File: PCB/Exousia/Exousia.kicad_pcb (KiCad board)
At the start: 2 copper layers, 73 parts, among them J1 IN/out, J2 I2C buss, J3 in/OUT, Q1 2N7002, Q2 2N7002, Q3 2N7002, U1 AON7410, U2 AON7410, U3 RVSPG, U4 AON7410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

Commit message: started layout of PCB, minus main inductor :C
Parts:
- moved R16 112.1 mm to (161.0, 218.4)
- moved JP4 108.2 mm to (168.4, 215.6), turned to 180 degrees
- moved JP3 105.1 mm to (160.5, 214.6), turned to 180 degrees
- moved R3 104.9 mm to (134.9, 206.0), turned to 270 degrees
- moved R8 104.4 mm to (143.3, 207.0), turned to 270 degrees
- moved Q2 99.5 mm to (143.0, 210.8)
- moved R11 96.7 mm to (151.9, 208.8), turned to 270 degrees
- moved JP1 96.5 mm to (125.7, 200.9)
- moved R12 96.0 mm to (154.4, 206.2), turned to 270 degrees
- moved R19 95.4 mm to (168.7, 218.7)
- moved Q1 92.6 mm to (133.9, 210.3)
- moved D1 90.2 mm to (137.4, 209.0), turned to 90 degrees
- moved D4 88.7 mm to (154.4, 210.8), turned to 90 degrees
- moved R15 87.3 mm to (160.5, 206.0), turned to 270 degrees
- moved R26 84.7 mm to (122.2, 173.5)
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
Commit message: did a little bit of layout
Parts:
- moved J2 59.6 mm to (180.8, 166.4), turned to 180 degrees
- moved R26 55.5 mm to (176.0, 160.0), turned to 270 degrees
- moved R27 52.3 mm to (177.8, 160.0), turned to 270 degrees
- moved JP1 39.9 mm to (137.7, 162.8)
- moved R16 39.3 mm to (168.1, 179.8)
- moved R19 39.0 mm to (172.2, 179.8)
- moved JP4 38.8 mm to (172.5, 177.0)
- moved Q3 38.3 mm to (159.8, 175.0)
- moved JP3 38.3 mm to (167.9, 177.0)
- moved R18 37.8 mm to (172.2, 169.2), turned to 0 degrees
- moved R15 37.6 mm to (168.1, 169.2), turned to 180 degrees
- moved R11 37.4 mm to (159.5, 172.2), turned to 180 degrees
- moved Q1 37.4 mm to (146.1, 175.0)
- moved Q2 37.2 mm to (152.9, 175.0)
- moved D4 36.3 mm to (163.1, 175.5)
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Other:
- board text added: "main chip U3 is wrong footprint"

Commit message: did work
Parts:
- removed TP1: RVSPG, TestPoint:TestPoint_Loop_D2.50mm_Drill1.0mm
- removed TP2: FRWPG, TestPoint:TestPoint_Loop_D2.50mm_Drill1.0mm
- added L1: 2uH, Inductor_SMD:L_6.3x6.3_H3, F.Cu at (159.5, 147.3)
- D1, D3: value LED -> FRWPG
- D4: value LED -> RVSPG
- J3: footprint Connector_PinSocket_2.54mm:PinSocket_1x02_P2.54mm_Vertical -> Connector_PinSocket_2.54mm:PinSocket_1x04_P2.54mm_Vertical
- JP1: value SolderJumper_3_Open -> IO-Vselect; footprint Connector_PinSocket_2.54mm:PinSocket_1x03_P2.54mm_Vertical -> Jumper:SolderJumper-3_P1.3mm_Open_RoundedPad1.0x1.5mm_NumberLabels
- JP2: value SolderJumper_3_Open -> Pin_FRWEN / ADP; footprint Connector_PinSocket_2.54mm:PinSocket_1x03_P2.54mm_Vertical -> Jumper:SolderJumper-3_P1.3mm_Open_RoundedPad1.0x1.5mm_NumberLabels
- JP3: value SolderJumper_3_Open -> RVSEN; footprint Connector_PinSocket_2.54mm:PinSocket_1x03_P2.54mm_Vertical -> Jumper:SolderJumper-3_P1.3mm_Open_RoundedPad1.0x1.5mm_NumberLabels
- JP4: value SolderJumper_3_Open -> Pin_FRWEN; footprint Connector_PinSocket_2.54mm:PinSocket_1x03_P2.54mm_Vertical -> Jumper:SolderJumper-3_P1.3mm_Open_RoundedPad1.0x1.5mm_NumberLabels
- moved JP1 10.3 mm to (145.5, 169.4)
- moved J1 7.15 mm to (133.3, 153.9), turned to 180 degrees
- moved J3 7.12 mm to (190.2, 153.9), turned to 180 degrees
- moved R19 3.89 mm to (171.4, 176.0), turned to 180 degrees
- moved R16 3.81 mm to (168.1, 176.0)
- moved JP2 3.39 mm to (149.9, 153.2), turned to 180 degrees
- moved JP3 3.34 mm to (167.4, 173.7)
- moved JP4 3.31 mm to (172.2, 173.7)
- moved R18 2.41 mm to (171.4, 171.4)
- moved R15 2.29 mm to (168.1, 171.4)
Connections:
- J1 pad 2: Net-(D2-Pad1) -> GND
- J1 pad 3: (no net) -> Net-(D2-Pad1)
- J1 pad 4: (no net) -> Net-(D2-Pad1)
- J3 pad 2: Net-(J3-Pad2) -> GND
- R24 pad 1: Net-(J3-Pad2) -> Net-(J3-Pad3)
- R25 pad 2: Net-(J3-Pad2) -> Net-(J3-Pad3)

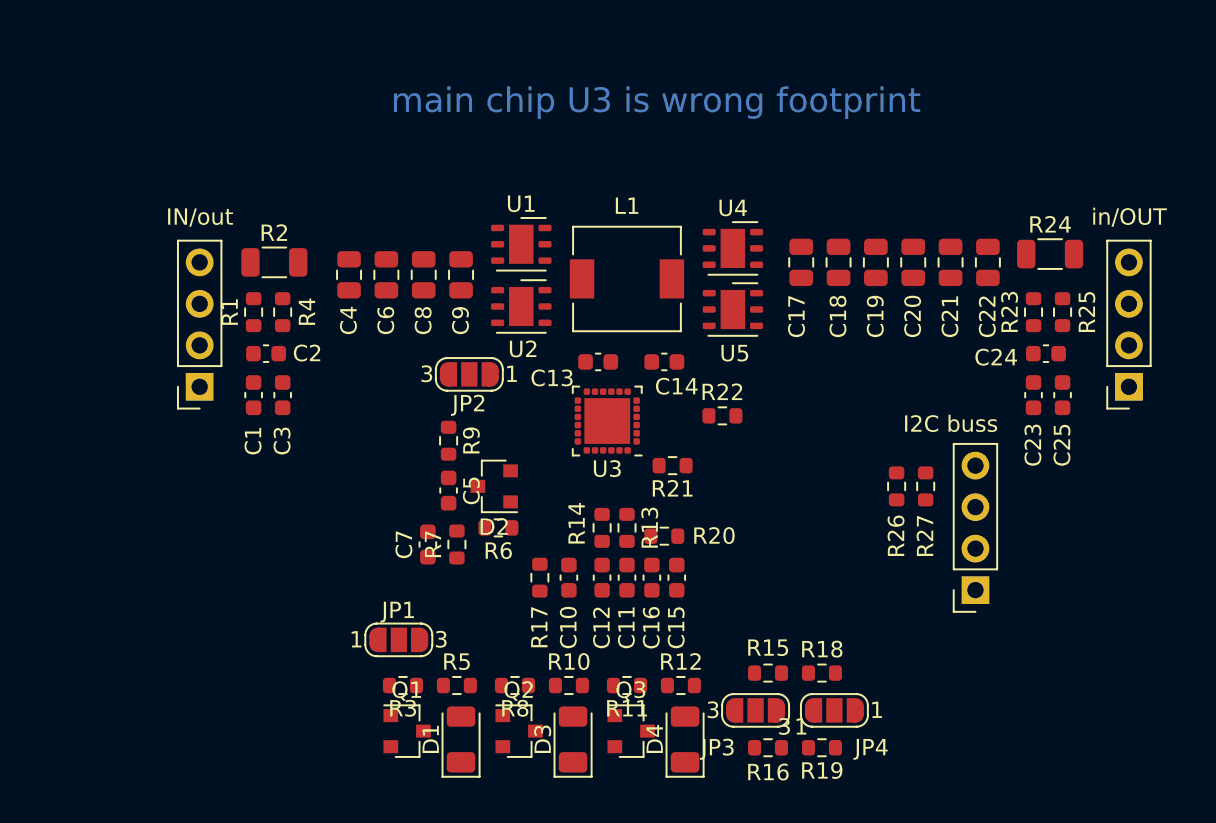
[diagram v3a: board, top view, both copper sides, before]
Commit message: updated some footrpints and compoinent valeus for 12A
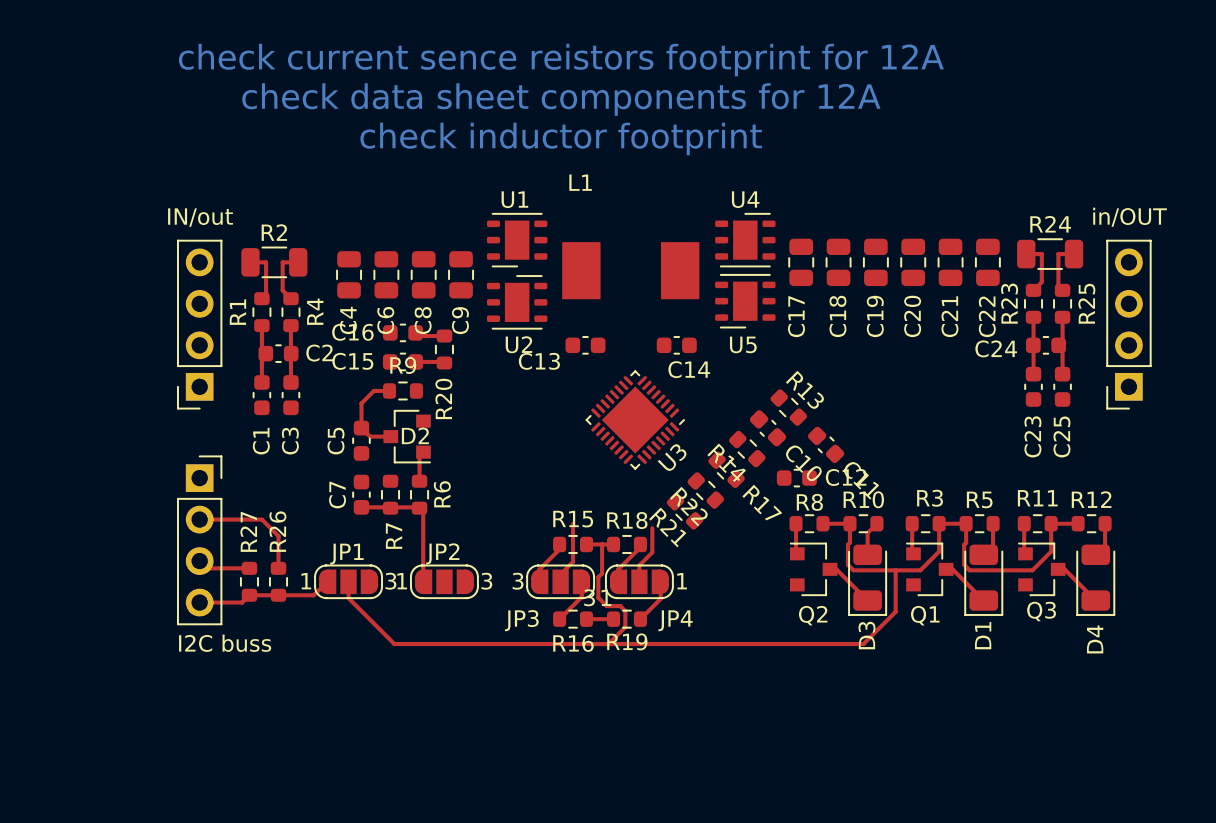
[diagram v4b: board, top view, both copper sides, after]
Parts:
- L1: value 2uH -> 0.82uH PIMB063T-R82MS-68; footprint Inductor_SMD:L_6.3x6.3_H3 -> PIMB063T-R82MS-68:PIMB063T-R82MS-68
- U3: footprint Package_DFN_QFN:TQFN-24-1EP_4x4mm_P0.5mm_EP2.8x2.8mm_PullBack -> Package_DFN_QFN:QFN-32-1EP_4x4mm_P0.4mm_EP2.9x2.9mm
- moved J2 48.0 mm to (133.3, 159.5), turned to 0 degrees
- moved R27 41.8 mm to (136.4, 165.9), turned to 90 degrees
- moved R26 38.3 mm to (138.2, 165.9), turned to 90 degrees
- moved R3 33.5 mm to (177.8, 162.3)
- moved D1 33.5 mm to (181.4, 165.6)
- moved Q1 33.5 mm to (178.1, 165.1)
- moved R5 33.5 mm to (181.1, 162.3)
- moved Q3 27.0 mm to (184.9, 165.1)
- moved R12 27.0 mm to (188.0, 162.3)
- moved D4 27.0 mm to (188.2, 165.6)
- moved R11 27.0 mm to (184.7, 162.3)
- moved C16 21.4 mm to (145.8, 150.6), turned to 180 degrees
- moved C15 21.3 mm to (145.8, 152.4), turned to 180 degrees
- moved Q2 20.6 mm to (170.9, 165.1)
- moved R10 20.6 mm to (174.0, 162.3)
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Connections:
- C10 pad 1: (no net) -> Net-(C10-Pad1)
- C15 pad 1: Net-(C15-Pad1) -> VDD
- JP1 pad 3: (no net) -> VDD
- R13 pad 1: (no net) -> Net-(R13-Pad1)
- R14 pad 1: (no net) -> Net-(R14-Pad1)
- R17 pad 1: (no net) -> Net-(R17-Pad1)
- R20 pad 2: Net-(C15-Pad1) -> VDD
- U3 pad 18: Net-(C15-Pad1) -> VDD
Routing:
- net Net-(JP1-Pad2): track 0.00 -> 74.5 mm
- net +3V3: track 0.00 -> 8.34 mm
- net Net-(C7-Pad1): track 0.00 -> 8.18 mm
- net SCL: track 0.00 -> 7.22 mm
- net Net-(C5-Pad1): track 0.00 -> 5.55 mm
- net Net-(D2-Pad1): track 0.00 -> 5.16 mm
- net RVSEN: track 0.00 -> 3.87 mm
- net Pin_FRWEN: track 0.00 -> 3.60 mm
- net Net-(C2-Pad1): track 0.00 -> 3.48 mm
- net Net-(C1-Pad2): track 0.00 -> 3.48 mm
- net Net-(C24-Pad1): track 0.00 -> 3.48 mm
- net Net-(C23-Pad2): track 0.00 -> 3.48 mm
- net Net-(C17-Pad1): track 0.00 -> 3.39 mm
- net Net-(C4-Pad1): track 0.00 -> 3.39 mm
- net Net-(J3-Pad3): track 0.00 -> 3.28 mm
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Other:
- board text added: "check current sence reistors footprint for 12A check data sheet components for 12A check inductor footprint"
- board text removed: "main chip U3 is wrong footprint"

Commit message: did routing!
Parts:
- moved C15 1.52 mm to (145.8, 153.9)
- moved C5 1.52 mm to (143.3, 158.8)
- moved C7 1.52 mm to (143.3, 162.1)
- moved D2 1.52 mm to (146.1, 158.5)
- moved R20 1.52 mm to (148.3, 153.2)
- moved R6 1.52 mm to (146.8, 162.1)
- moved R7 1.52 mm to (145.0, 162.1)
- moved R9 1.52 mm to (145.8, 155.7)
- moved C16 1.52 mm to (145.8, 152.1)
- moved J3 0.72 mm to (189.7, 153.4)
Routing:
- net Net-(U1-Pad4): track 0.00 -> 18.5 mm, vias 0 -> 2
- net Net-(C17-Pad1): track 3.39 -> 21.8 mm, vias 0 -> 2
- net Net-(U3-Pad5): track 0.00 -> 15.5 mm, vias 0 -> 2
- net Net-(D2-Pad1): track 5.16 -> 16.1 mm
- net Net-(C13-Pad1): track 0.00 -> 10.1 mm
- net Net-(U3-Pad7): track 0.00 -> 8.68 mm
- net Net-(U2-Pad4): track 0.00 -> 8.30 mm
- net Net-(R13-Pad1): track 0.00 -> 8.18 mm
- net GND: track 1.65 -> 9.41 mm, vias 0 -> 47
- net Net-(C14-Pad1): track 0.00 -> 7.56 mm
- net Net-(C10-Pad1): track 0.00 -> 6.88 mm
- net Net-(R14-Pad1): track 0.00 -> 5.57 mm
- net FRWPG: track 1.88 -> 6.83 mm
- net Net-(C7-Pad1): track 8.18 -> 3.51 mm
- net Net-(R17-Pad1): track 0.00 -> 4.34 mm
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- added copper zone on B.Cu, net GND
- added copper zone on F.Cu, net GND
- added copper zone on F.Cu, net Net-(C13-Pad1)
- added copper zone on F.Cu, net Net-(C14-Pad1)
- added copper zone on F.Cu, net Net-(C17-Pad1)
- added copper zone on F.Cu, net Net-(C4-Pad1)
- added copper zone on F.Cu, net Net-(D2-Pad1)
- added copper zone on F.Cu, net Net-(J3-Pad3)
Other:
- net class Default: clearance 0.2 -> 0.127
- rule trace_clearance: 0.2 -> 0.127

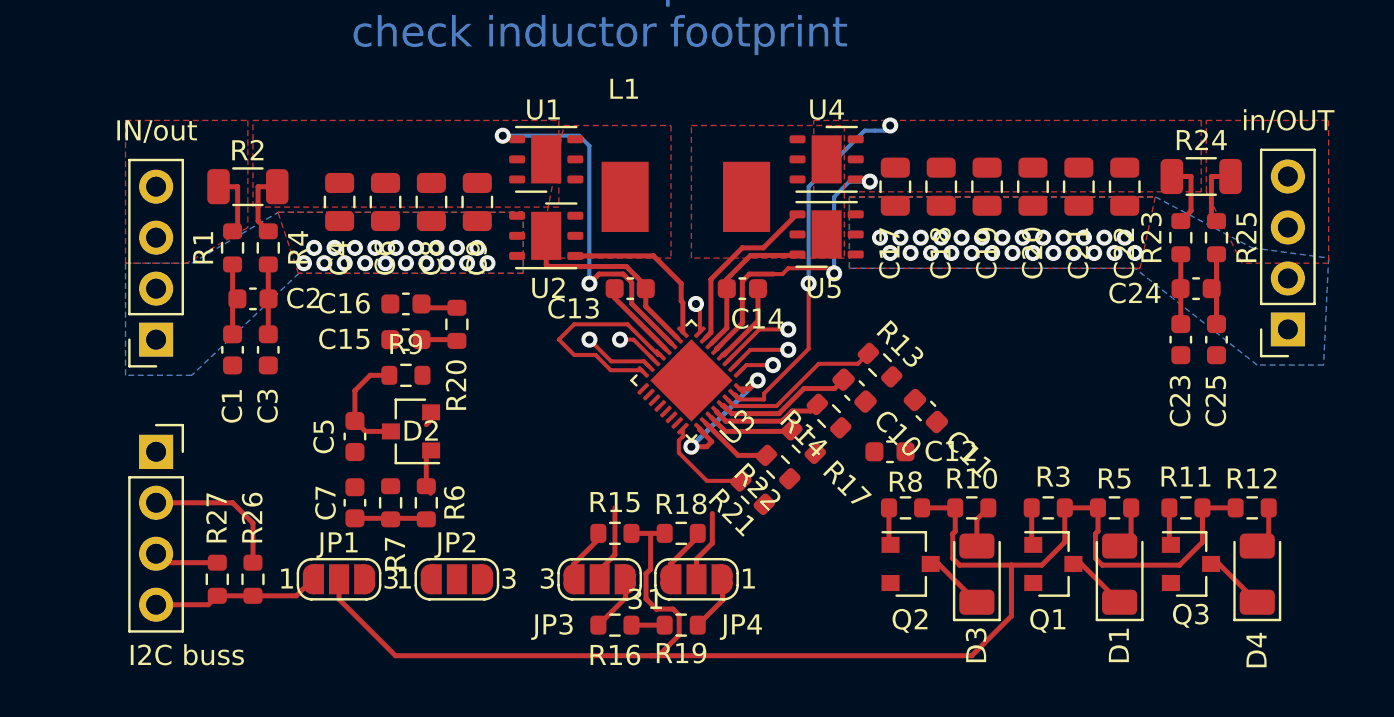
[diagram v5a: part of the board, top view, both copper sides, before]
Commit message: finished most of the routing
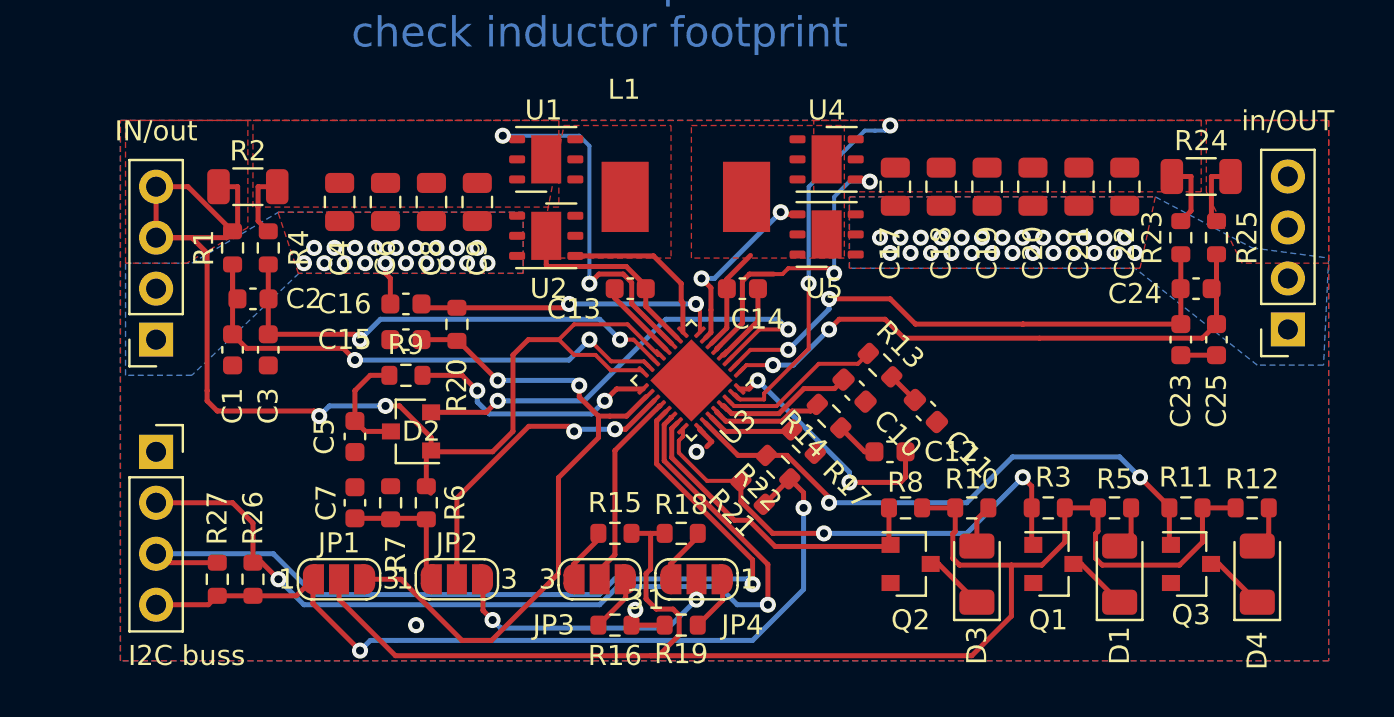
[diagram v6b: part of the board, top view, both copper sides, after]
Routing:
- net Net-(D2-Pad1): track 16.1 -> 61.4 mm, vias 0 -> 2
- net SDA: track 3.23 -> 45.8 mm, vias 0 -> 1
- net SCL: track 7.22 -> 46.1 mm, vias 0 -> 2
- net +3V3: track 8.34 -> 43.8 mm, vias 0 -> 2
- net VDD: track 1.70 -> 34.6 mm, vias 0 -> 2
- net Net-(C24-Pad1): track 5.28 -> 29.4 mm, vias 1 -> 2
- net RVSPG: track 5.57 -> 28.8 mm, vias 0 -> 2
- net Net-(C23-Pad2): track 6.52 -> 28.0 mm, vias 1 -> 2
- net Net-(C1-Pad2): track 6.99 -> 27.5 mm, vias 1 -> 2
- net Net-(D2-Pad2): track 3.97 -> 23.6 mm, vias 1 -> 2
- net FRWPG: track 6.83 -> 25.4 mm, vias 0 -> 2
- net Net-(C2-Pad1): track 5.63 -> 24.1 mm, vias 1 -> 2
- net Net-(JP2-Pad2): track 0.00 -> 16.9 mm, vias 0 -> 2
- net PROCHOT#: track 1.88 -> 16.5 mm
- net DCIN: track 0.00 -> 12.6 mm, vias 0 -> 2
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
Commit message: minor changes to the PCB
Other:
- board text added: "check current sence reistors footprint for 12A check data sheet components for 12A check inductor footprint IC gnd pad ? ground or thermal ?"
- board text removed: "check current sence reistors footprint for 12A check data sheet components for 12A check inductor footprint"
